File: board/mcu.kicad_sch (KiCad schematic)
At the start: 50 parts, among them IC1 PMV48XP, J1 USB-B-S-X-X-TH, J10 AVR-ISP-6, J8 AVR-ISP-6, U2 LMV358IDT, U3 ATmega2560-16A, U4 LD1117S50TR_SOT223, U5 LP2985-3.3, U6 ATmega16U2-A, Y1 CSTCE16M0V53-R0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

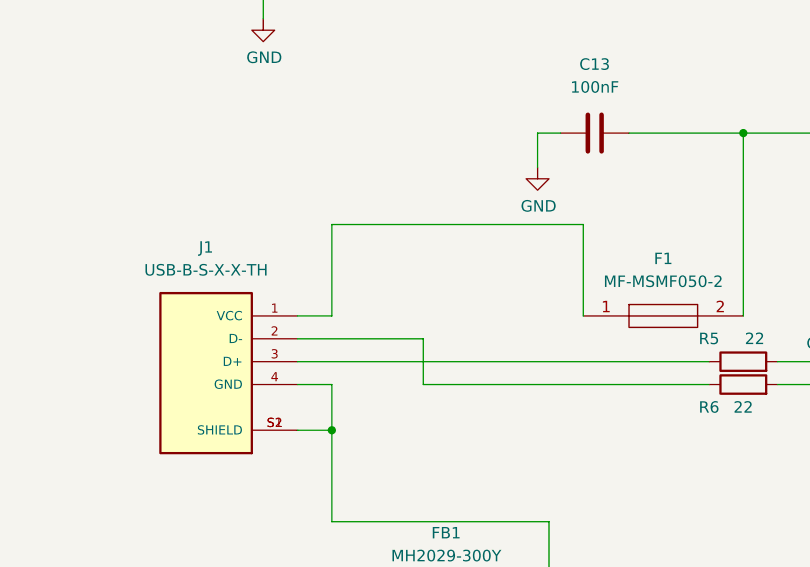
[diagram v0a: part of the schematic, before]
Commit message: Completed routing
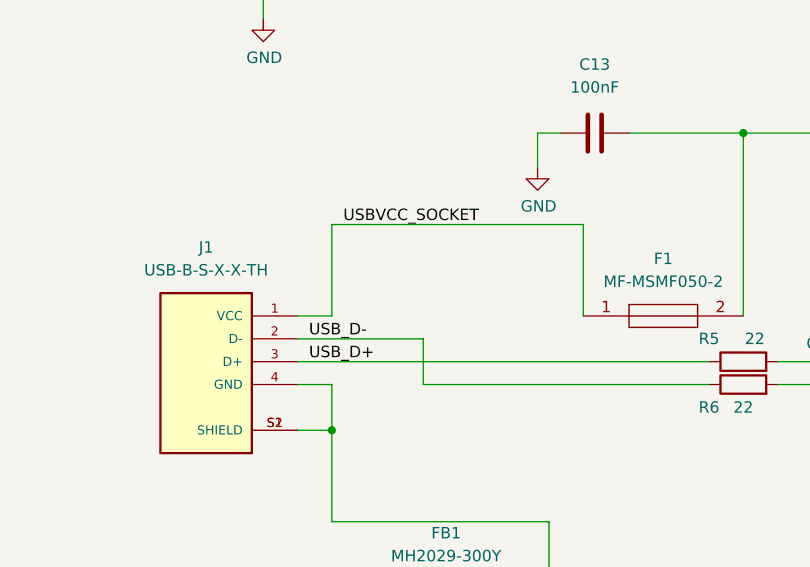
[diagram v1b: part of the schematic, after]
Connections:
- net USB_D+: now reaches J1.3 (D+), R5.1
- net USB_D-: now reaches J1.2 (D-), R6.1
- net USBVCC_SOCKET: now reaches F1.1, J1.1 (VCC)
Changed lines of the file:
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@@
     (stroke (width 0) (type default) (color 0 0 0 0))
+  )
+  (label "USB_D-" (at 222.25 82.55 0)
+    (effects (font (size 1.27 1.27)) (justify left bottom))
+  )
+  (label "USBVCC_SOCKET" (at 226.06 69.85 0)
+    (effects (font (size 1.27 1.27)) (justify left bottom))
+  )
+  (label "USB_D+" (at 222.25 85.09 0)
+    (effects (font (size 1.27 1.27)) (justify left bottom))
   )
   (global_label "TX0" (shape bidirectional) (at 330.2 170.18 180) (fields_autoplaced)

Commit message: tested LCD, button scan and serial output
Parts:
- C1, C13, C17, C18, C2, C3, C4, C5, C6, C7: Farnell Part Number (none) -> 1907331; Manufacturer_Name (none) -> TDK; Manufacturer_Part_Number (none) -> C2012X7R2A104K125AA
- C10, C8, C9: Farnell Part Number (none) -> 2211186; Manufacturer_Name (none) -> TDK; Manufacturer_Part_Number (none) -> C2012X5R1A476M125AC
- C11, C14, C15: Farnell Part Number (none) -> 1759195; Manufacturer_Name (none) -> MULTICOMP PRO; Manufacturer_Part_Number (none) -> MC0805N220J500CT
- C12, C16: Farnell Part Number (none) -> 2346940; Manufacturer_Name (none) -> TDK; Manufacturer_Part_Number (none) -> C2012X7R1E105K125AB
- D13, D14: Digi-Key Part Number (none) -> CD1206-B2100CT-ND
- D15, D16: Farnell Part Number (none) -> 3796323; Manufacturer_Name (none) -> MULTICOMP PRO; Manufacturer_Part_Number (none) -> MP008291
- F1: Digi-Key Part Number (none) -> MF-MSMF050-2CT-ND
- FB1: Farnell Part Number (none) -> 2859248
- IC1: Farnell Part Number (none) -> 3361018
- J1: Digi-Key Part Number (none) -> SAM9008-ND; Manufacturer_Name (none) -> Samtec; Manufacturer_Part_Number (none) -> USB-B-S-S-W-TH
- J10, J8: Digi-Key Part Number (none) -> 90130-1206
- L1: Farnell Part Number (none) -> 2286571; Manufacturer_Name (none) -> COILCRAFT; Manufacturer_Part_Number (none) -> 0805PS-103KRC
- R1: Farnell Part Number (none) -> 2145441; Manufacturer_Name (none) -> PANASONIC; Manufacturer_Part_Number (none) -> ERJU06F1004V
- R10, R11, R12, R8, R9: Farnell Part Number (none) -> 2073606; Manufacturer_Name (none) -> MULTICOMP PRO; Manufacturer_Part_Number (none) -> MCMR08X1001FTL
- R2, R3, R4, R7: Farnell Part Number (none) -> 1652909; Manufacturer_Name (none) -> VISHAY; Manufacturer_Part_Number (none) -> CRCW080510K0FKTA
- R5, R6: Farnell Part Number (none) -> 1099789; Manufacturer_Name (none) -> TT ELECTRONICS / WELWYN; Manufacturer_Part_Number (none) -> WCR0805-22RFI
- U2: Digi-Key Part Number (none) -> 497-4945-1-ND
- U3: Farnell Part Number (none) -> 1288330; Manufacturer_Name (none) -> MICROCHIP; Manufacturer_Part_Number (none) -> ATMEGA2560-16AU
- U4: Farnell Part Number (none) -> 1467781; Manufacturer_Name (none) -> STMICROELECTRONICS; Manufacturer_Part_Number (none) -> LD1117S50TR
- U5: Farnell Part Number (none) -> 3007620; Manufacturer_Name (none) -> TEXAS INSTRUMENTS; Manufacturer_Part_Number (none) -> LP2985A-33DBVT
- U6: Farnell Part Number (none) -> 1841607; Manufacturer_Name (none) -> MICROCHIP; Manufacturer_Part_Number (none) -> ATMEGA16U2-AU
- Y1: Digi-Key Part Number (none) -> 490-17949-1-ND
- Y2: Digi-Key Part Number (none) -> 1923-1788-ND; Manufacturer_Name (none) -> IQD Frequency Products; Manufacturer_Part_Number (none) -> LFXTAL027945BULK

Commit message: updated to Crane V2 Rev A
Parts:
- removed C1, C13, C17, C18, C4, C5, C6, C7: 100nF, Capacitor_SMD:C_0805_2012Metric, symbol Device:C
- removed C10, C8, C9: 47uF, Capacitor_SMD:C_0805_2012Metric, symbol Device:C
- removed C11, C14, C15: 22pF, Capacitor_SMD:C_0805_2012Metric, symbol Device:C
- removed C12: 1uF, Capacitor_SMD:C_0805_2012Metric, symbol Device:C
- removed D13, D14: CD1206-S01575, footprints:DIOC3215X95N, symbol CD1206-S01575:CD1206-S01575
- removed D15: LED_RX, LED_SMD:LED_0805_2012Metric, symbol Device:LED
- removed D16: LED_TX, LED_SMD:LED_0805_2012Metric, symbol Device:LED
- removed F1: MF-MSMF050-2, footprints:FUSC4632X85N, symbol MF-MSMF050-2:MF-MSMF050-2
- removed FB1: MH2029-300Y, footprints:BEADC2016X130N, symbol MH2029-300Y:MH2029-300Y
- removed IC1: PMV48XP, footprints:SOT95P230X110-3N, symbol PMV48XP:PMV48XP
- removed J1: USB-B-S-X-X-TH, SAMTEC_USB-B-S-X-X-TH, symbol USB-B-S-X-X-TH:USB-B-S-X-X-TH
- removed J10, J8: AVR-ISP-6, Connector_IDC:IDC-Header_2x03_P2.54mm_Vertical, symbol Connector:AVR-ISP-6
- removed JP1: GROUND, Jumper:SolderJumper-2_P1.3mm_Bridged_RoundedPad1.0x1.5mm, symbol Jumper:SolderJumper_2_Bridged
- removed JP2: RESET-EN, Jumper:SolderJumper-2_P1.3mm_Bridged_RoundedPad1.0x1.5mm, symbol Jumper:SolderJumper_2_Bridged
- removed L1: 10uH, Inductor_SMD:L_0805_2012Metric, symbol Device:L
- removed R1: 1M, Resistor_SMD:R_0805_2012Metric, symbol Device:R
- removed R10, R11, R12, R8, R9: 1K, Resistor_SMD:R_0805_2012Metric, symbol Device:R
- removed R2, R3, R4, R7: 10K, Resistor_SMD:R_0805_2012Metric, symbol Device:R
- removed R5, R6: 22, Resistor_SMD:R_0805_2012Metric, symbol Device:R
- removed U2: LMV358IDT, Package_SO:SO-8_3.9x4.9mm_P1.27mm, symbol Amplifier_Operational:LM358
- removed U3: ATmega2560-16A, Package_QFP:TQFP-100_14x14mm_P0.5mm, symbol MCU_Microchip_ATmega:ATmega2560-16A
- removed U4: LD1117S50TR_SOT223, Package_TO_SOT_SMD:SOT-223-3_TabPin2, symbol Regulator_Linear:LD1117S50TR_SOT223
- removed U5: LP2985-3.3, Package_TO_SOT_SMD:SOT-23-5, symbol Regulator_Linear:LP2985-3.3
- removed U6: ATmega16U2-A, Package_QFP:TQFP-32_7x7mm_P0.8mm, symbol MCU_Microchip_ATmega:ATmega16U2-A
- removed Y1: CSTCE16M0V53-R0, footprints:CSTCE16M0V53R0, symbol CSTCE16M0V53-R0:CSTCE16M0V53-R0
- removed Y2: Crystal, Crystal:Crystal_HC49-4H_Vertical, symbol Device:Crystal
- added FB1: HZ0805E601R-10, Inductor_SMD:L_0805_2012Metric, symbol Device:FerriteBead
- added J16: Conn_01x02_Male, Connector_PinHeader_2.54mm:PinHeader_1x02_P2.54mm_Horizontal, symbol Connector_Generic:Conn_01x02
- added R18, R19: 10K, Resistor_SMD:R_0805_2012Metric, symbol Device:R
- added R18: 100, Resistor_SMD:R_0805_2012Metric, symbol Device:R
- added SW13: SW_Push_DPDT, Button_Switch_THT:SW_CuK_JS202011CQN_DPDT_Straight, symbol Switch:SW_Push_DPDT
- added SW14: SW_Push, Button_Switch_THT:SW_PUSH_6mm_H9.5mm, symbol Switch:SW_Push
- added U1: STM32L476RGT6, Package_QFP:LQFP-64_10x10mm_P0.5mm, symbol MCU_ST_STM32L4:STM32L496RGTx
- added e1: 9B-16.000MAAE-B, Crystal:Crystal_HC49-U_Vertical, symbol Device:Crystal_Small
- C16: value 1uF -> 100nF; Digi-Key Part Number (none) -> 1276-1003-1-ND; Farnell Part Number 2346940 -> (none); LCSC (none) -> C1711; MANUFACTURER (none) -> Samsung; Manufacturer_Name TDK -> Samsung; Manufacturer_Part_Number C2012X7R1E105K125AB -> CL21B104KBCNNNC
- C2, C3: value 100nF -> 20pF; Digi-Key Part Number (none) -> 1276-1829-1-ND; Farnell Part Number 1907331 -> (none); LCSC (none) -> C1798; MANUFACTURER (none) -> Samsung; Manufacturer_Name TDK -> Samsung; Manufacturer_Part_Number C2012X7R2A104K125AA -> CL21C200JBANNNC
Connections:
- net +3V3: now also FB1.1, R18.1, U1.1 (VBAT), U1.19 (VDD), U1.32 (VDD), U1.48 (VDDUSB), U1.64 (VDD)
- net GND: now also C16.1, J16.1 (Pin_1), R18.1, R19.2, U1.12 (VSSA), U1.18 (VSS), U1.31 (VSS), U1.47 (VSS), U1.63 (VSS)
- net LCD_BL: now also U1.26 (PB0)
- net LCD_CLK: now also U1.21 (PA5)
- net LCD_CS: now also U1.20 (PA4)
- net LCD_DC: now also U1.24 (PC4)
- net LCD_DIN: now also U1.23 (PA7)
- net LCD_RST: now also U1.25 (PC5)
- net SW_C0: now also U1.37 (PC6)
- net SW_C1: now also U1.38 (PC7)
- net SW_C2: now also U1.39 (PC8)
- net SW_R0: now also U1.33 (PB12)
- net SW_R1: now also U1.34 (PB13)
- net SW_R2: now also U1.35 (PB14)
- net SW_R3: now also U1.36 (PB15)
- net at C2.2: now also U1.5 (PH0), e1.1
- net NRST: now reaches C16.2
- net NRST: now also J16.2 (Pin_2), SW14.2, U1.7 (NRST)
- net at C3.2: now also U1.6 (PH1), e1.2
- new net: R18.2, SW13.1 (A)
- new net: R19.1, SW13.3 (C)
- new net: R18.2, SW14.1
- new net: FB1.2, U1.13 (VDDA)
- new net BOOT0: SW13.2 (B), U1.60 (PH3)
- new net I2C_SCL: U1.58 (PB6)
- new net I2C_SDA: U1.59 (PB7)
- new net JTCK_SWCLK: U1.49 (PA14)
- new net JTDO_SWO: U1.55 (PB3)
- new net JTMS_SWDIO: U1.46 (PA13)
- new net SPI_MISO: U1.10 (PC2)
- new net SPI_MOSI: U1.11 (PC3)
- new net SPI_NSS: U1.62 (PB9)
- new net SPI_SCK: U1.29 (PB10)
- new net USART_RX: U1.43 (PA10)
- new net USART_TX: U1.42 (PA9)
- new net USB_OTG_FS_D+: U1.45 (PA12)
- new net USB_OTG_FS_D-: U1.44 (PA11)

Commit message: removed software folder
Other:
- title: (none) -> Crane V2.0 Rev A
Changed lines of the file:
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@@
 (kicad_sch (version 20230121) (generator eeschema)
   (paper "A3")
+  (title_block
+    (title "Crane V2.0 Rev A")
+  )
   (junction (at 187.96 137.16) (diameter 0) (color 0 0 0 0)
   )
